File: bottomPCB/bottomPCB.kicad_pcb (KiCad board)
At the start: 2 copper layers, 184.8 x 132.4 mm, 53 parts, among them CN2 XT30UPB-F, J2 Conn_02x03_Odd_Even, J3 Conn_01x02, J4 Conn_02x03_Odd_Even, U1 ESP32-WROOM-32, U3 XT30_horizontal, U8 LM1117IMPX-3_3_NOPB, U9 LM1117IMPX-3_3_NOPB

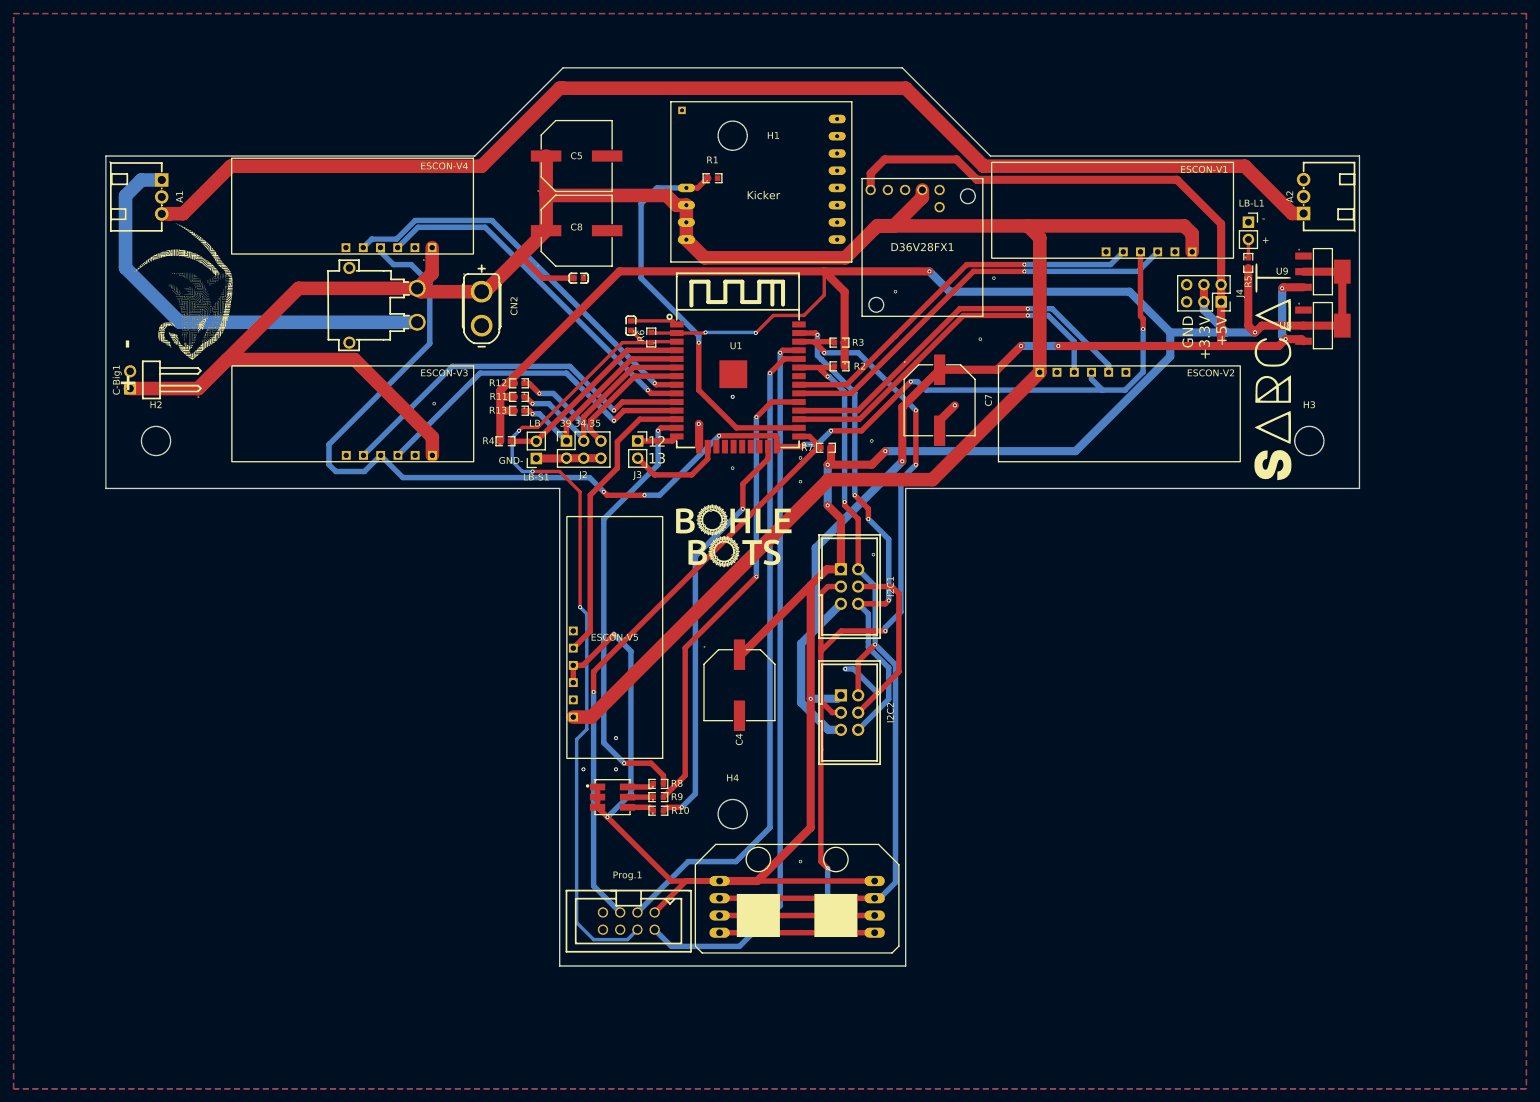
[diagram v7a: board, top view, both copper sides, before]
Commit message: moved Connectors to accomodate vertical drivers
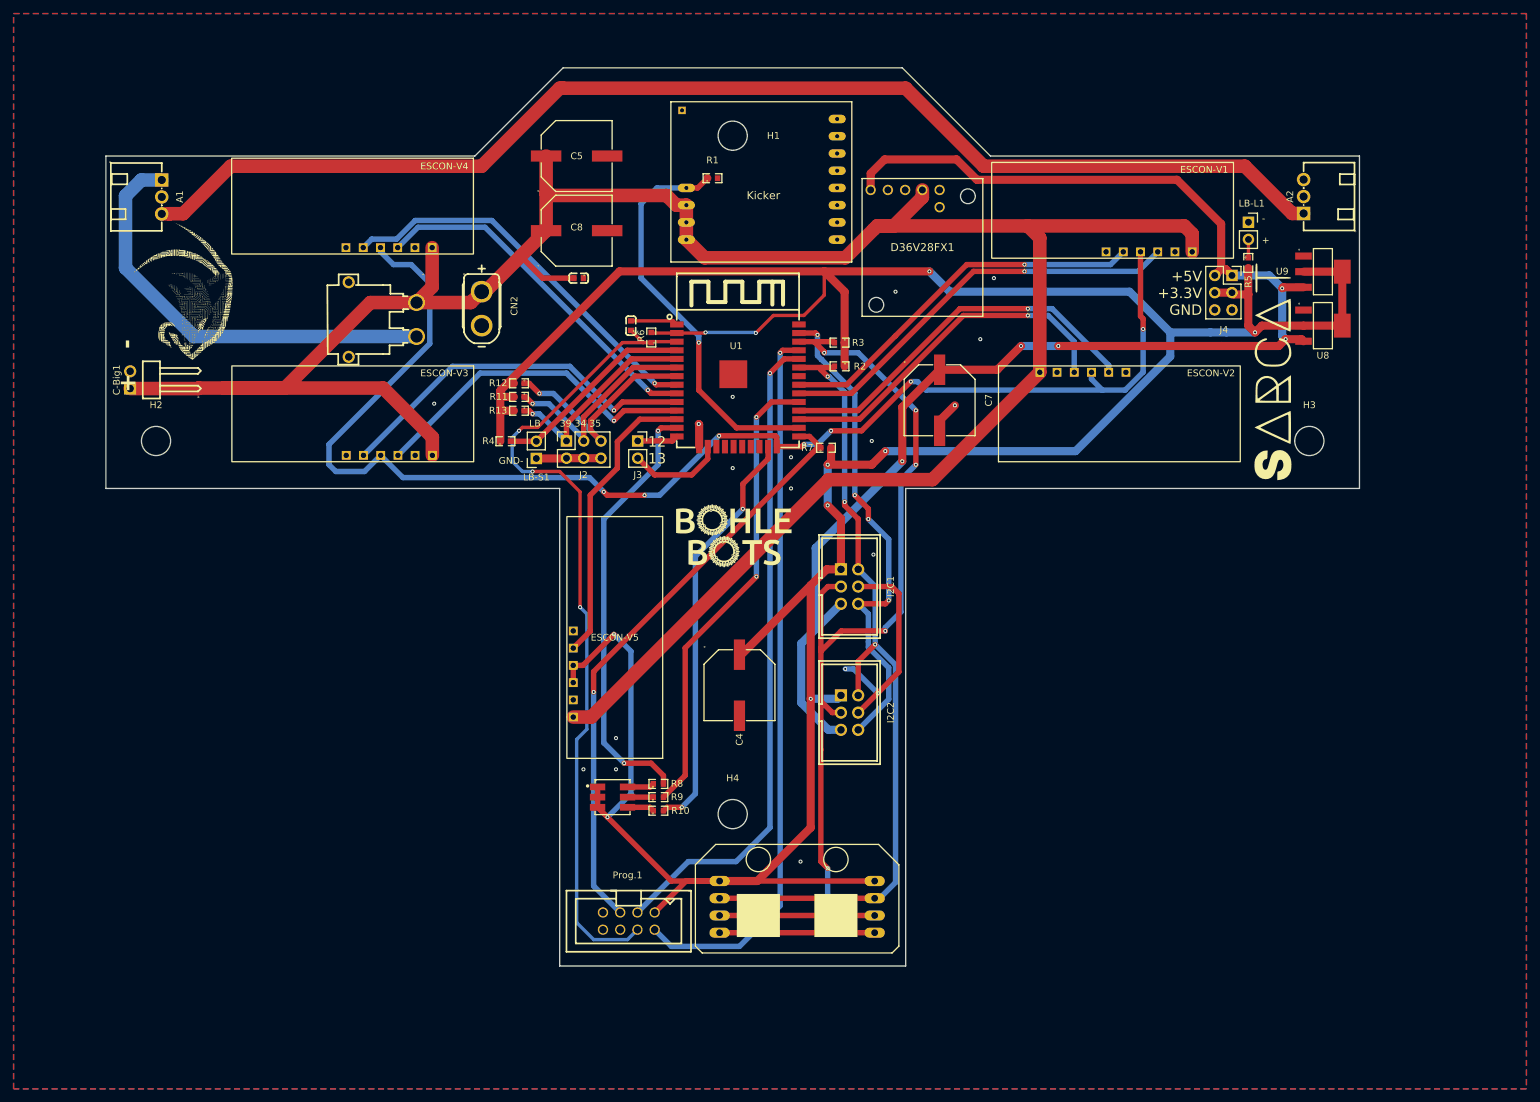
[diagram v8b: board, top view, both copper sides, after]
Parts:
- moved J4 4.22 mm to (83.6, 0.60), turned to 0 degrees
- moved U3 2.10 mm to (-41.6, 7.10)
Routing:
- net +BATT: track 371.7 -> 366.1 mm
- net +3.3V: track 483.3 -> 479.9 mm
- net Net-(A1-Pad1): track 63.3 -> 64.0 mm
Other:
- board text added: "+5V +3.3V GND"
- board text removed: "GND +3.3V +5V"
